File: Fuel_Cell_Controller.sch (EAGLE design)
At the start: 57 parts, among them U1 MAX232PTH

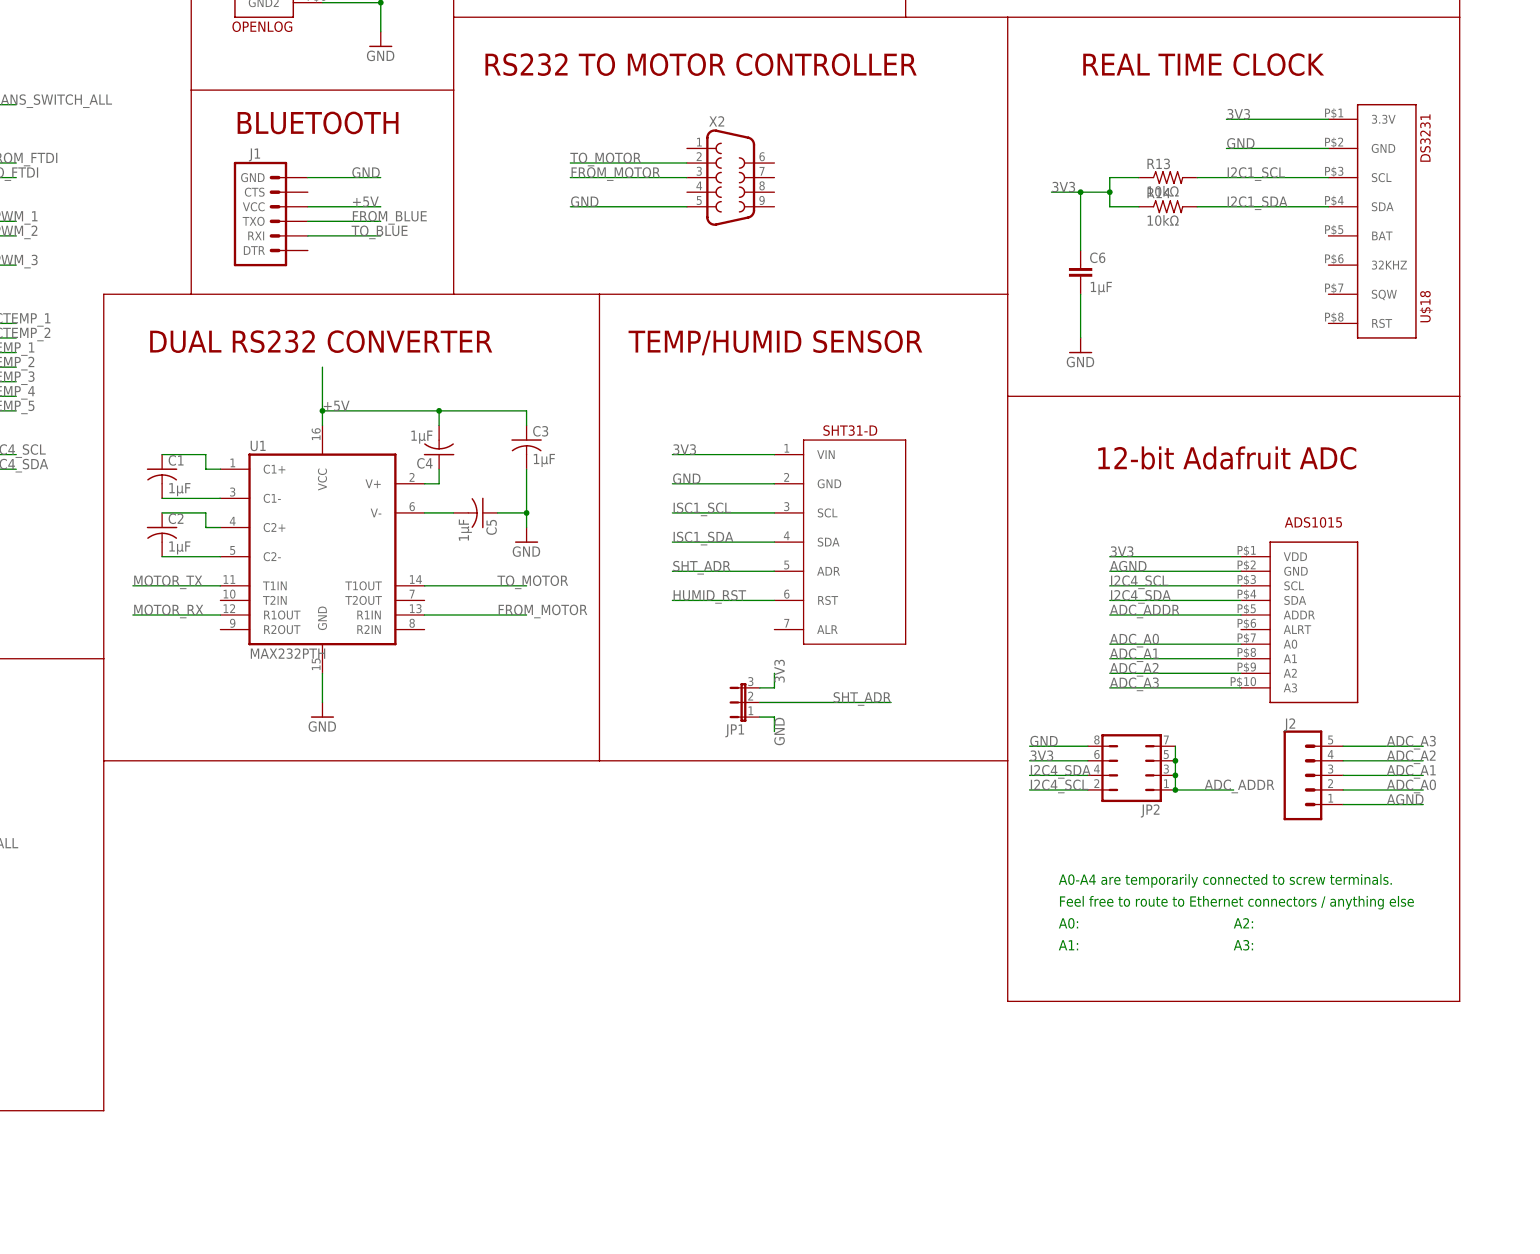
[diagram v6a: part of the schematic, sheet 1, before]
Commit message: Working on routing now. Deleted caps and resistors on RTC
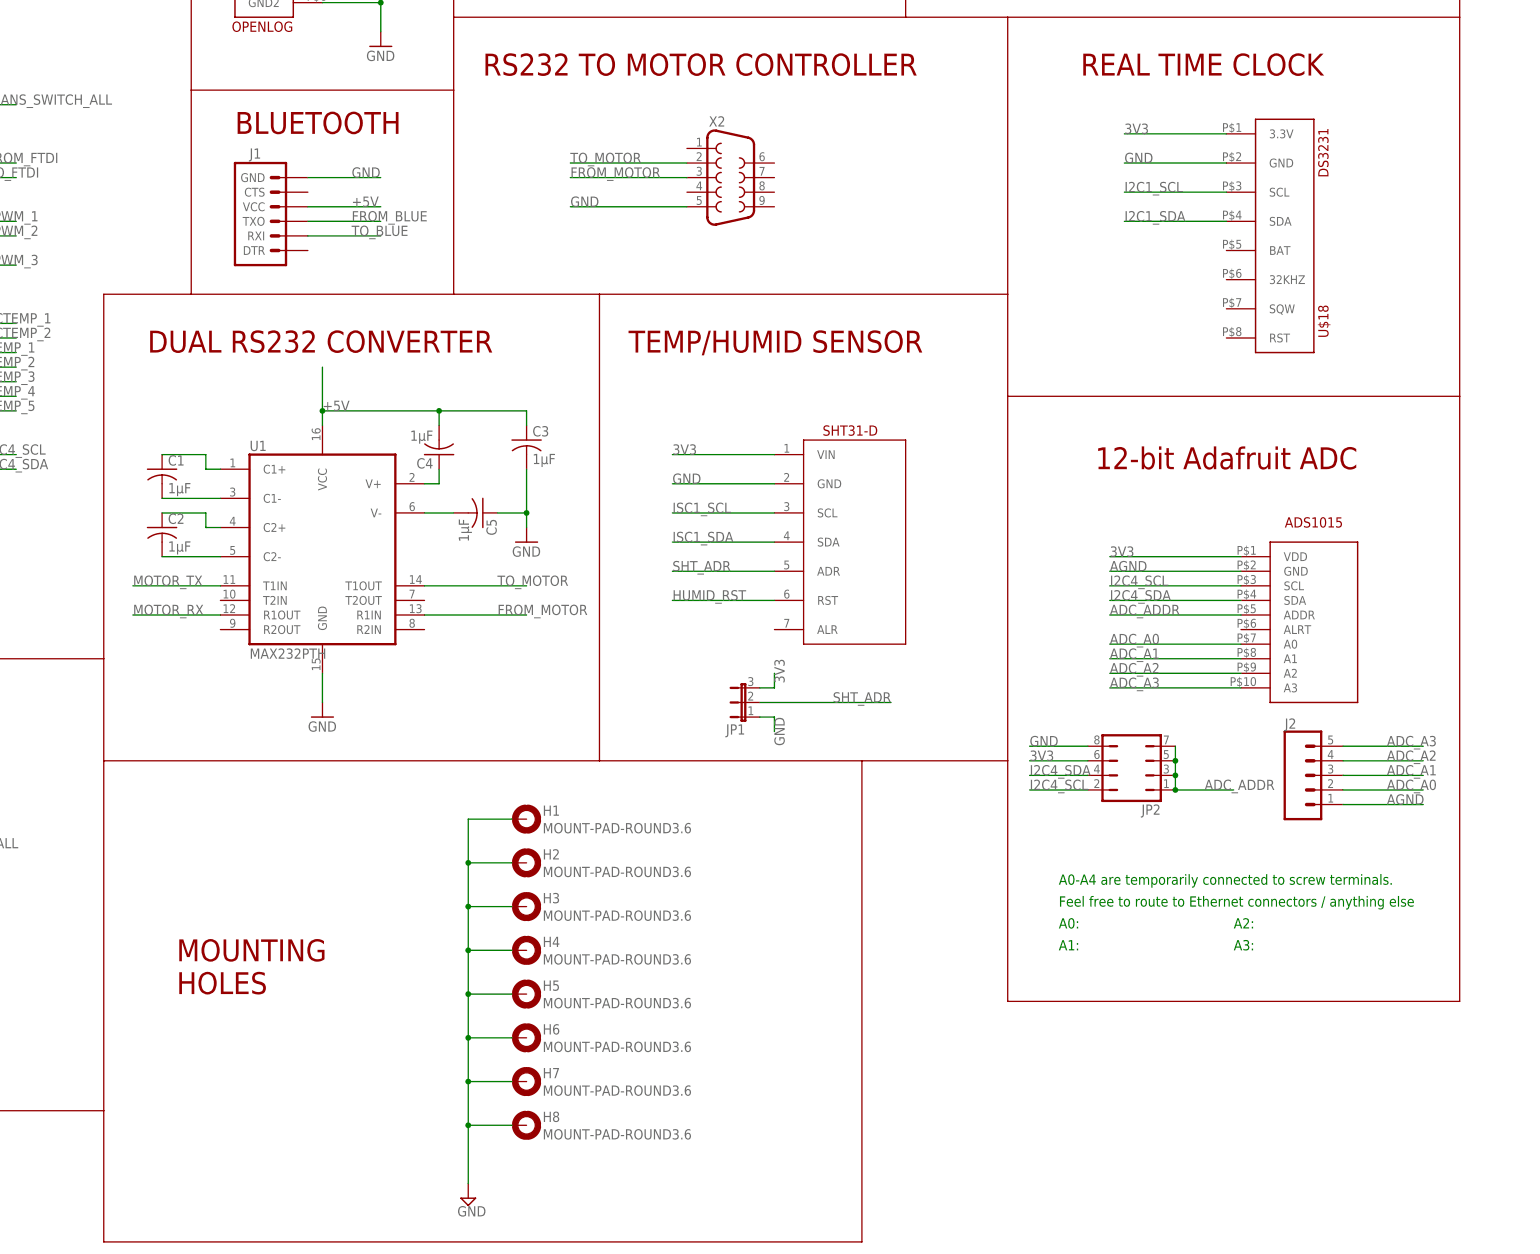
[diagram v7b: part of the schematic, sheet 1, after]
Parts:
- removed C6: 1µF, SparkFun-Capacitors:CAP0603-CAP
- removed R13, R14: 10kΩ, SparkFun-Resistors:RESISTOR0603
- added H1, H2, H3, H4, H5, H6, H7, H8: MOUNT-PAD-ROUND3.6, holes:MOUNT-PAD-ROUND3.6
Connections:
- net 3V3: no longer C6.1, R13.1, R14.1
- net GND: now also H1.MOUNT, H2.MOUNT, H3.MOUNT, H4.MOUNT, H5.MOUNT, H6.MOUNT, H7.MOUNT, H8.MOUNT; no longer C6.2
- net I2C1_SCL: no longer R13.2
- net I2C1_SDA: no longer R14.2
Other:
- note added: "MOUNTING HOLES"
- moved on the sheet: U$18
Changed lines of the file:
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@@
 <?xml version="1.0" encoding="utf-8"?>
 <!DOCTYPE eagle SYSTEM "eagle.dtd">
-<eagle version="8.4.1">
+<eagle version="8.3.2">
 <drawing>
 <settings>
@@
 <part name="X1" library="con-subd" library_urn="urn:adsk.eagle:library:189" deviceset="F09" device="HP" package3d_urn="urn:adsk.eagle:package:10232/1"/>
 <part name="U$18" library="DS3231" deviceset="DS3231" device=""/>
-<part name="R13" library="SparkFun-Resistors" deviceset="RESISTOR" device="0603" value="10kΩ"/>
-<part name="R14" library="SparkFun-Resistors" deviceset="RESISTOR" device="0603" value="10kΩ"/>
-<part name="C6" library="SparkFun-Capacitors" deviceset="CAP" device="0603-CAP" value="1µF"/>
-<part name="GND4" library="E-P-008-R1.2" deviceset="GND" device=""/>
 <part name="U$19" library="FCC_parts" deviceset="ADS1015" device=""/>
 <part name="JP2" library="jumper" library_urn="urn:adsk.eagle:library:252" deviceset="JP4Q" device="" package3d_urn="urn:adsk.eagle:package:15451/1"/>
 <part name="J2" library="SparkFun-Connectors" library_urn="urn:adsk.eagle:library:513" deviceset="CONN_05" device="SCREW" package3d_urn="urn:adsk.eagle:package:38112/1"/>
+<part name="H1" library="holes" library_urn="urn:adsk.eagle:library:237" deviceset="MOUNT-PAD-ROUND" device="3.6" package3d_urn="urn:adsk.eagle:package:14284/1"/>
+<part name="H2" library="holes" library_urn="urn:adsk.eagle:library:237" deviceset="MOUNT-PAD-ROUND" device="3.6" package3d_urn="urn:adsk.eagle:package:14284/1"/>
+<part name="H3" library="holes" library_urn="urn:adsk.eagle:library:237" deviceset="MOUNT-PAD-ROUND" device="3.6" package3d_urn="urn:adsk.eagle:package:14284/1"/>
+<part name="H4" library="holes" library_urn="urn:adsk.eagle:library:237" deviceset="MOUNT-PAD-ROUND" device="3.6" package3d_urn="urn:adsk.eagle:package:14284/1"/>
+<part name="H5" library="holes" library_urn="urn:adsk.eagle:library:237" deviceset="MOUNT-PAD-ROUND" device="3.6" package3d_urn="urn:adsk.eagle:package:14284/1"/>
+<part name="H6" library="holes" library_urn="urn:adsk.eagle:library:237" deviceset="MOUNT-PAD-ROUND" device="3.6" package3d_urn="urn:adsk.eagle:package:14284/1"/>
+<part name="H7" library="holes" library_urn="urn:adsk.eagle:library:237" deviceset="MOUNT-PAD-ROUND" device="3.6" package3d_urn="urn:adsk.eagle:package:14284/1"/>
+<part name="H8" library="holes" library_urn="urn:adsk.eagle:library:237" deviceset="MOUNT-PAD-ROUND" device="3.6" package3d_urn="urn:adsk.eagle:package:14284/1"/>
+<part name="SUPPLY1" library="supply2" library_urn="urn:adsk.eagle:library:372" deviceset="GND" device=""/>
 </parts>
 <sheets>
@@
 <wire x1="281.94" y1="-15.24" x2="210.82" y2="-15.24" width="0.1524" layer="94"/>
 <text x="215.9" y="-25.4" size="3.81" layer="94">TEMP/HUMID SENSOR</text>
-<wire x1="210.82" y1="-96.52" x2="281.94" y2="-96.52" width="0.1524" layer="94"/>
+<wire x1="210.82" y1="-96.52" x2="256.54" y2="-96.52" width="0.1524" layer="94"/>
+<wire x1="256.54" y1="-96.52" x2="281.94" y2="-96.52" width="0.1524" layer="94"/>
 <wire x1="281.94" y1="-96.52" x2="281.94" y2="-33.02" width="0.1524" layer="94"/>
 <text x="271.78" y="68.58" size="3.81" layer="94">RS232 TO MASS FLOW METER</text>
@@
 <text x="321.31" y="-125.73" size="1.778" layer="91">A2:</text>
 <text x="321.31" y="-129.54" size="1.778" layer="91">A3:</text>
+<text x="137.16" y="-137.16" size="3.81" layer="94">MOUNTING
+HOLES</text>
+<wire x1="124.46" y1="-157.48" x2="124.46" y2="-180.34" width="0.1524" layer="94"/>
+<wire x1="124.46" y1="-180.34" x2="256.54" y2="-180.34" width="0.1524" layer="94"/>
+<wire x1="256.54" y1="-180.34" x2="256.54" y2="-96.52" width="0.1524" layer="94"/>
 </plain>
 <instances>
@@
 <instance part="R2" gate="G$1" x="40.64" y="-99.06"/>
 <instance part="X1" gate="G$1" x="299.72" y="50.8"/>
-<instance part="U$18" gate="G$1" x="342.9" y="-2.54"/>
-<instance part="R13" gate="G$1" x="309.88" y="5.08"/>
-<instance part="R14" gate="G$1" x="309.88" y="0"/>
-<instance part="C6" gate="G$1" x="294.64" y="-12.7"/>
-<instance part="GND4" gate="1" x="294.64" y="-25.4"/>
+<instance part="U$18" gate="G$1" x="325.12" y="-5.08"/>
 <instance part="U$19" gate="G$1" x="322.58" y="-81.28"/>
 <instance part="JP2" gate="B" x="303.53" y="-99.06" rot="R90"/>
 <instance part="J2" gate="G$1" x="332.74" y="-99.06"/>
+<instance part="H1" gate="G$1" x="198.12" y="-106.68"/>
+<instance part="H2" gate="G$1" x="198.12" y="-114.3"/>
+<instance part="H3" gate="G$1" x="198.12" y="-121.92"/>
+<instance part="H4" gate="G$1" x="198.12" y="-129.54"/>
+<instance part="H5" gate="G$1" x="198.12" y="-137.16"/>
+<instance part="H6" gate="G$1" x="198.12" y="-144.78"/>
+<instance part="H7" gate="G$1" x="198.12" y="-152.4"/>
+<instance part="H8" gate="G$1" x="198.12" y="-160.02"/>
+<instance part="SUPPLY1" gate="GND" x="187.96" y="-172.72"/>
 </instances>
 <busses>
@@
 <segment>
 <pinref part="U$18" gate="G$1" pin="GND"/>
-<wire x1="337.82" y1="10.16" x2="320.04" y2="10.16" width="0.1524" layer="91"/>
-<label x="320.04" y="10.16" size="1.778" layer="95"/>
-</segment>
-<segment>
-<pinref part="C6" gate="G$1" pin="2"/>
-<wire x1="294.64" y1="-15.24" x2="294.64" y2="-22.86" width="0.1524" layer="91"/>
-<pinref part="GND4" gate="1" pin="GND"/>
+<wire x1="320.04" y1="7.62" x2="302.26" y2="7.62" width="0.1524" layer="91"/>
+<label x="302.26" y="7.62" size="1.778" layer="95"/>
 </segment>
 <segment>
@@
 <wire x1="295.91" y1="-93.98" x2="285.75" y2="-93.98" width="0.1524" layer="91"/>
 <label x="285.75" y="-93.98" size="1.778" layer="95"/>
+</segment>
+<segment>
+<pinref part="H1" gate="G$1" pin="MOUNT"/>
+<wire x1="195.58" y1="-106.68" x2="187.96" y2="-106.68" width="0.1524" layer="91"/>
+<wire x1="187.96" y1="-106.68" x2="187.96" y2="-114.3" width="0.1524" layer="91"/>
+<pinref part="H8" gate="G$1" pin="MOUNT"/>
+<wire x1="187.96" y1="-114.3" x2="187.96" y2="-121.92" width="0.1524" layer="91"/>
+<wire x1="187.96" y1="-121.92" x2="187.96" y2="-129.54" width="0.1524" layer="91"/>
+<wire x1="187.96" y1="-129.54" x2="187.96" y2="-137.16" width="0.1524" layer="91"/>
+<wire x1="187.96" y1="-137.16" x2="187.96" y2="-144.78" width="0.1524" layer="91"/>
+<wire x1="187.96" y1="-144.78" x2="187.96" y2="-152.4" width="0.1524" layer="91"/>
+<wire x1="187.96" y1="-152.4" x2="187.96" y2="-160.02" width="0.1524" layer="91"/>
+<wire x1="187.96" y1="-160.02" x2="187.96" y2="-170.18" width="0.1524" layer="91"/>
+<wire x1="195.58" y1="-160.02" x2="187.96" y2="-160.02" width="0.1524" layer="91"/>
+<junction x="187.96" y="-160.02"/>
+<pinref part="H7" gate="G$1" pin="MOUNT"/>
+<wire x1="195.58" y1="-152.4" x2="187.96" y2="-152.4" width="0.1524" layer="91"/>
+<junction x="187.96" y="-152.4"/>
+<pinref part="H6" gate="G$1" pin="MOUNT"/>
+<wire x1="195.58" y1="-144.78" x2="187.96" y2="-144.78" width="0.1524" layer="91"/>
+<junction x="187.96" y="-144.78"/>
+<pinref part="H5" gate="G$1" pin="MOUNT"/>
+<wire x1="195.58" y1="-137.16" x2="187.96" y2="-137.16" width="0.1524" layer="91"/>
+<junction x="187.96" y="-137.16"/>
+<pinref part="H4" gate="G$1" pin="MOUNT"/>
+<wire x1="195.58" y1="-129.54" x2="187.96" y2="-129.54" width="0.1524" layer="91"/>
+<junction x="187.96" y="-129.54"/>
+<pinref part="H3" gate="G$1" pin="MOUNT"/>
+<wire x1="195.58" y1="-121.92" x2="187.96" y2="-121.92" width="0.1524" layer="91"/>
+<junction x="187.96" y="-121.92"/>
+<pinref part="H2" gate="G$1" pin="MOUNT"/>
+<wire x1="195.58" y1="-114.3" x2="187.96" y2="-114.3" width="0.1524" layer="91"/>
+<junction x="187.96" y="-114.3"/>
+<pinref part="SUPPLY1" gate="GND" pin="GND"/>
 </segment>
 </net>
@@
 <segment>
 <pinref part="U$18" gate="G$1" pin="3.3V"/>
-<wire x1="337.82" y1="15.24" x2="320.04" y2="15.24" width="0.1524" layer="91"/>
-<label x="320.04" y="15.24" size="1.778" layer="95"/>
-</segment>
-<segment>
-<pinref part="R14" gate="G$1" pin="1"/>
-<wire x1="304.8" y1="0" x2="299.72" y2="0" width="0.1524" layer="91"/>
-<wire x1="299.72" y1="0" x2="299.72" y2="2.54" width="0.1524" layer="91"/>
-<wire x1="299.72" y1="2.54" x2="294.64" y2="2.54" width="0.1524" layer="91"/>
-<pinref part="R13" gate="G$1" pin="1"/>
-<wire x1="294.64" y1="2.54" x2="289.56" y2="2.54" width="0.1524" layer="91"/>
-<wire x1="304.8" y1="5.08" x2="299.72" y2="5.08" width="0.1524" layer="91"/>
-<wire x1="299.72" y1="5.08" x2="299.72" y2="2.54" width="0.1524" layer="91"/>
-<junction x="299.72" y="2.54"/>
-<label x="289.56" y="2.54" size="1.778" layer="95"/>
-<pinref part="C6" gate="G$1" pin="1"/>
-<wire x1="294.64" y1="2.54" x2="294.64" y2="-7.62" width="0.1524" layer="91"/>
-<junction x="294.64" y="2.54"/>
+<wire x1="320.04" y1="12.7" x2="302.26" y2="12.7" width="0.1524" layer="91"/>
+<label x="302.26" y="12.7" size="1.778" layer="95"/>
 </segment>
 <segment>
@@
 <segment>
 <pinref part="U$18" gate="G$1" pin="SCL"/>
-<pinref part="R13" gate="G$1" pin="2"/>
-<wire x1="337.82" y1="5.08" x2="314.96" y2="5.08" width="0.1524" layer="91"/>
-<label x="320.04" y="5.08" size="1.778" layer="95"/>
+<wire x1="320.04" y1="2.54" x2="302.26" y2="2.54" width="0.1524" layer="91"/>
+<label x="302.26" y="2.54" size="1.778" layer="95"/>
 </segment>
 </net>
@@
 <segment>
 <pinref part="U$18" gate="G$1" pin="SDA"/>
-<wire x1="337.82" y1="0" x2="314.96" y2="0" width="0.1524" layer="91"/>
-<label x="320.04" y="0" size="1.778" layer="95"/>
-<pinref part="R14" gate="G$1" pin="2"/>
-</segment>
-<segment>
+<wire x1="320.04" y1="-2.54" x2="302.26" y2="-2.54" width="0.1524" layer="91"/>
+<label x="302.26" y="-2.54" size="1.778" layer="95"/>
+</segment>
+<segment>

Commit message: lol kk
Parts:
- removed ETH9: ETHERNET, ETHERNET:ETHERNET
- added ETH5: ETHERNET, ETHERNET:ETHERNET
- J1: value (none) -> BLUETOOTH; device SparkFun-Connectors:ARDUINO_SERIAL_PROGRAMPTH -> FCC_parts:BLUETOOTH
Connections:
- removed net AGND: ETH1.7, ETH4.8, J2.1, U$1.AGND, U$19.GND, X1.2
- removed net ISC1_SCL: SHTSENSOR.SCL
- removed net ISC1_SDA: SHTSENSOR.SDA
- net ESTOP_1: now also ETH5.3; no longer ETH6.3
- net ESTOP_2: now also ETH5.4; no longer ETH6.4
- net FAN1_PWR: now also ETH6.1; no longer ETH7.1
- net FAN2_PWR: now also ETH6.4; no longer ETH7.4
- net FAN3_PWR: now also ETH7.1; no longer ETH8.1
- net GND: now also ETH1.7, ETH4.8, ETH5.5, ETH5.6, ETH5.7, ETH5.8, ETH5.SHD1, ETH5.SHD2, ETH8.2, ETH8.4, ETH8.6, J2.1, U$1.AGND, U$19.GND, X1.2; no longer ETH6.5, ETH6.6, ETH6.7, ETH9.2, ETH9.4, ETH9.6, ETH9.8, ETH9.SHD1, ETH9.SHD2
- net H2_OK: now also ETH5.2; no longer ETH6.2
- net I2C1_SCL: now also SHTSENSOR.SCL
- net I2C1_SDA: now also SHTSENSOR.SDA
- net OUTPUT_1_ENET: now also ETH8.5; no longer ETH9.5
- net OUTPUT_2_ENET: now also ETH8.7; no longer ETH9.7
- net PURGE_VALVE_ENET: now also ETH8.3; no longer ETH9.3
- net PWM_1: now also ETH6.3; no longer ETH7.3
- net PWM_2: now also ETH6.6; no longer ETH7.6
- net PWM_3: now also ETH7.3; no longer ETH8.3
- net STOP: now also ETH5.1; no longer ETH6.1
- net SUPPLY_VALVE_ENET: now also ETH8.1; no longer ETH9.1
- net TACH_1: now also ETH6.2; no longer ETH7.2
- net TACH_2: now also ETH6.5; no longer ETH7.5
- net TACH_3: now also ETH7.2; no longer ETH8.2
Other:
- moved on the sheet: ETH6, ETH7, ETH8
